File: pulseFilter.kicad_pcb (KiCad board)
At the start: 2 copper layers, 72 x 47 mm, 25 parts, among them U1 TMU_3-1213, U3 NJM2903D, U4 LDK320ADU120R

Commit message: update
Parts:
- added C7: 0, Capacitor_SMD:C_0603_1608Metric, F.Cu at (145.4, 80.2)
- added C8: 0, Capacitor_SMD:C_0603_1608Metric, F.Cu at (142.5, 83.2)
- added R10: 0, Resistor_THT:R_Axial_DIN0204_L3.6mm_D1.6mm_P7.62mm_Horizontal, F.Cu at (154.3, 85.3)
- added R9: 0, Resistor_THT:R_Axial_DIN0204_L3.6mm_D1.6mm_P7.62mm_Horizontal, F.Cu at (154.3, 82.8)
- C5: value 1u -> 0.1u
- moved RV1 5.68 mm to (155.6, 100.6), turned to 0 degrees
- moved C5 2.68 mm to (161.5, 98.8)
- moved R8 2.04 mm to (184.0, 98.0)
- moved C6 1.60 mm to (161.4, 93.9)
- moved C4 1.48 mm to (147.9, 91.5)
- moved C3 1.16 mm to (138.0, 93.5)
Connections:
- R1 pad 2: PULSE2 -> Net-(R1-Pad2)
- R2 pad 2: PULSE1 -> Net-(R2-Pad2)
- R5 pad 2: PULSE1 -> Net-(R2-Pad2)
- R6 pad 2: PULSE2 -> Net-(R1-Pad2)
- RV1 pad 1: 12V -> GND
- RV1 pad 3: GND -> 12V
- U3 pad 1: PULSE1 -> Net-(R2-Pad2)
- U3 pad 7: PULSE2 -> Net-(R1-Pad2)
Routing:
- net PULSE1: track 50.1 -> 9.02 mm
- net Net-(R2-Pad2): track 0.00 -> 37.5 mm
- net PULSE2: track 43.4 -> 13.8 mm
- net Net-(R1-Pad2): track 0.00 -> 23.3 mm
- net 12V: track 88.4 -> 95.1 mm
- net PULSE1_RAW: track 26.6 -> 24.6 mm
- net VREF: track 28.2 -> 30.0 mm
- net PULSE2_RAW: track 12.5 -> 13.4 mm
- net GND: vias 0 -> 75

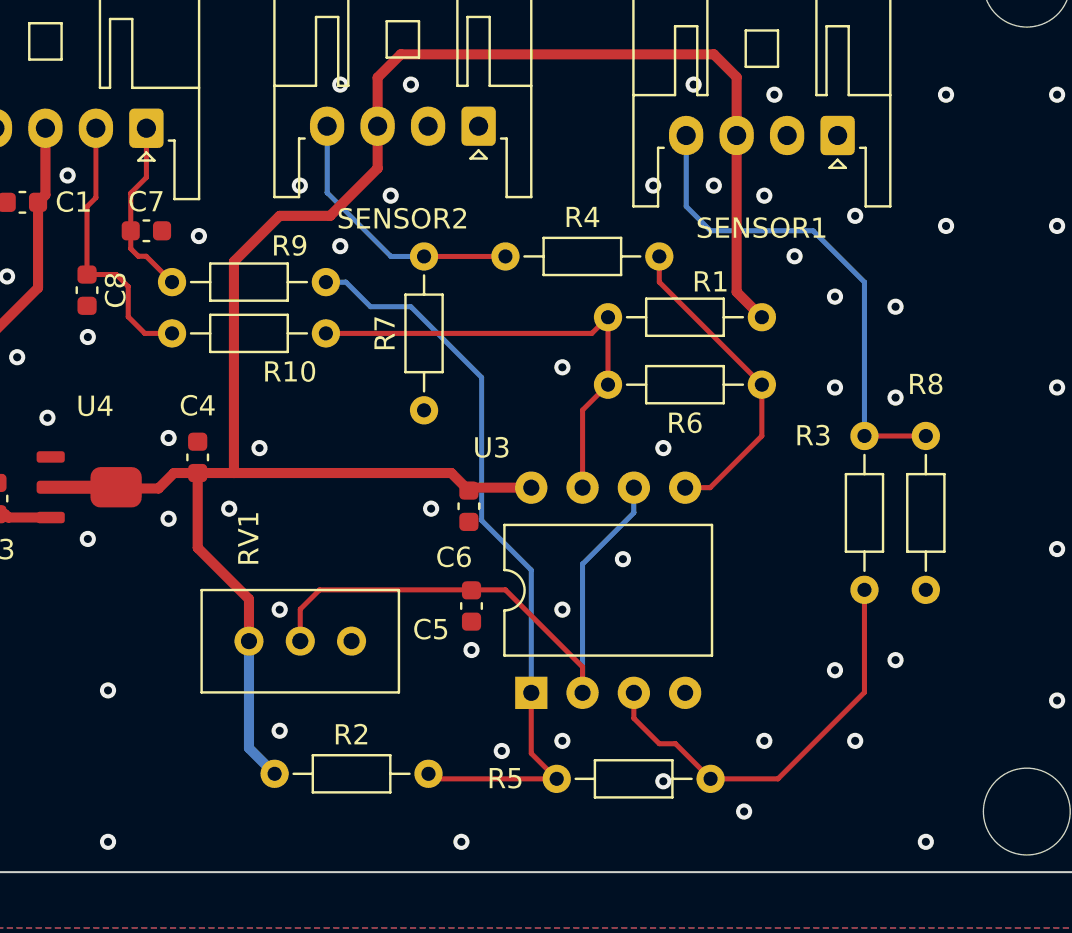
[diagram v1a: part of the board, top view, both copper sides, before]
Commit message: to chip resistors
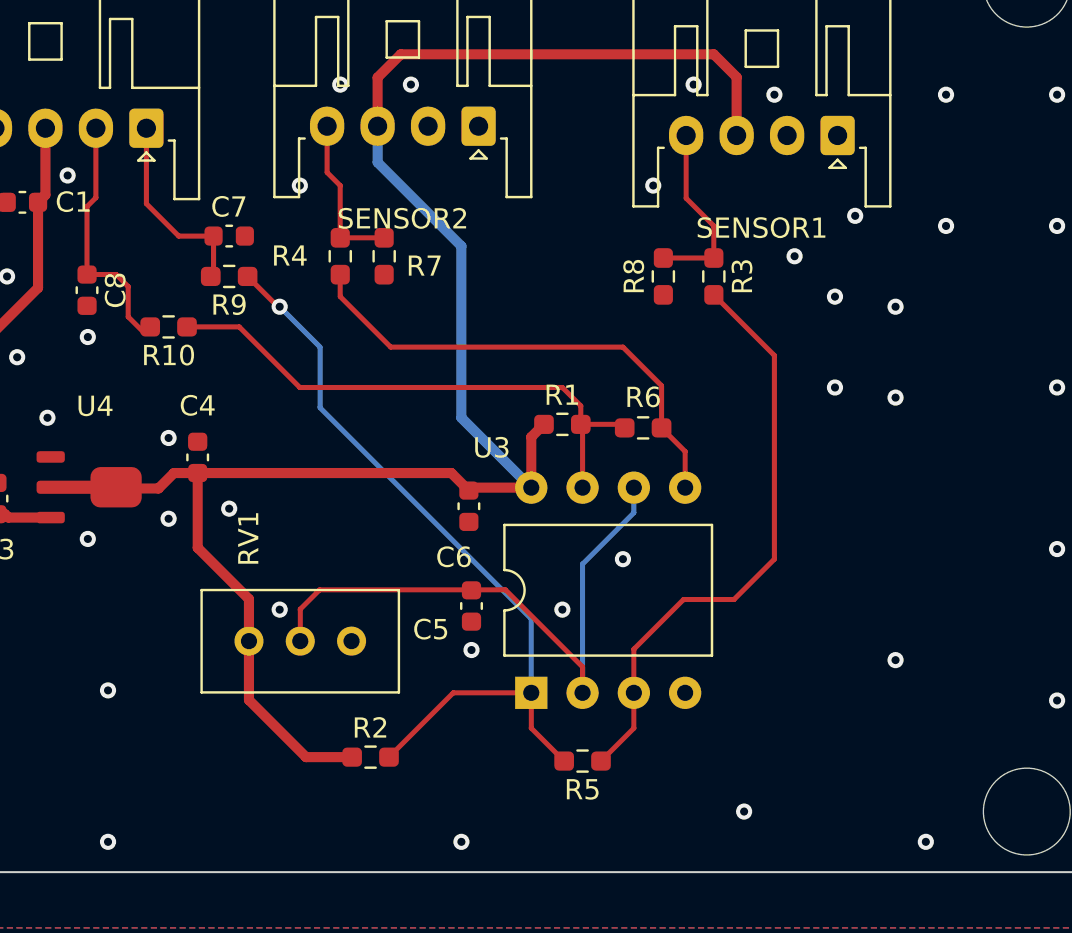
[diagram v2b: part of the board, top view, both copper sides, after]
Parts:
- R1, R10, R2, R3, R4, R5, R6, R7, R8, R9: footprint Resistor_THT:R_Axial_DIN0204_L3.6mm_D1.6mm_P7.62mm_Horizontal -> Resistor_SMD:R_0603_1608Metric_Pad0.98x0.95mm_HandSolder
- moved R8 20.2 mm to (171.0, 82.5)
- moved R1 11.2 mm to (166.0, 89.8), turned to 0 degrees
- moved R3 10.9 mm to (173.5, 82.5)
- moved R4 8.18 mm to (155.0, 81.5), turned to -90 degrees
- moved R7 7.88 mm to (157.2, 81.5)
- moved R10 7.80 mm to (146.5, 85.0)
- moved R5 6.40 mm to (167.0, 106.5)
- moved R6 6.26 mm to (170.0, 90.0)
- moved R2 4.82 mm to (156.5, 106.3)
- moved R9 4.80 mm to (149.5, 82.5)
- moved C7 4.11 mm to (149.5, 80.5)
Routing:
- net PULSE1_RAW: track 24.6 -> 9.13 mm
- net Net-(R3-Pad2): track 20.8 -> 29.4 mm
- net Net-(R4-Pad2): track 15.9 -> 24.4 mm
- net PULSE2_RAW: track 13.4 -> 7.97 mm
- net 12V: track 95.1 -> 90.5 mm
- net Net-(R1-Pad2): track 23.3 -> 27.5 mm
- net Net-(R2-Pad2): track 37.5 -> 38.9 mm, vias 0 -> 1
- net PULSE2: track 13.8 -> 12.4 mm
- net PULSE1: track 9.02 -> 9.78 mm
- net GND: vias 75 -> 59

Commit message: backup
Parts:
- added TP1: TestPoint, TestPoint:TestPoint_Loop_D1.80mm_Drill1.0mm_Beaded, F.Cu at (154.0, 95.0)
- C1, C2, C3, C4, C5, C6, C7, C8: footprint Capacitor_SMD:C_0603_1608Metric -> Capacitor_SMD:C_0603_1608Metric_Pad1.08x0.95mm_HandSolder
- moved R2 3.63 mm to (159.8, 104.8)
- moved C1 3.37 mm to (139.1, 82.2)
- moved R10 2.49 mm to (144.5, 83.5), turned to 90 degrees
- moved C2 1.82 mm to (135.3, 88.2)
- moved SENSOR1 1.71 mm to (178.0, 75.0)
- moved R7 1.70 mm to (157.1, 83.2)
- moved R4 1.70 mm to (155.0, 83.2)
- moved R8 0.40 mm to (171.4, 82.5)
- moved C8 0.32 mm to (142.5, 83.5)
- moved R1 0.17 mm to (166.0, 90.0)
- moved SENSOR2 0.06 mm to (161.8, 75.0)
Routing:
- net VREF: track 30.0 -> 34.1 mm
- net Net-(R2-Pad2): track 38.9 -> 35.3 mm
- net Net-(R1-Pad2): track 27.5 -> 30.6 mm
- net PULSE2: track 12.4 -> 10.2 mm
- net VBAT12V: track 20.9 -> 22.8 mm
- net PULSE2_RAW: track 7.97 -> 9.60 mm
- net PULSE1_RAW: track 9.13 -> 9.93 mm
- net Net-(R4-Pad2): track 24.4 -> 23.7 mm
- net 12V: track 90.5 -> 90.2 mm, vias 0 -> 1
- net GND: vias 59 -> 72
- net (no net): vias 0 -> 53
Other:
- rule pad_to_mask_clearance: 0 -> 0.1
- board text added: "12V"
- board text added: "BAT"
- board text added: "GND"
- board text added: "NC"
- board text added: "PUL1"
- board text added: "PUL2"
- board text added: "VREF"
